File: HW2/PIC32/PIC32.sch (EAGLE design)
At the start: 23 parts, among them J4 AMP FCI 10103594-0001LF

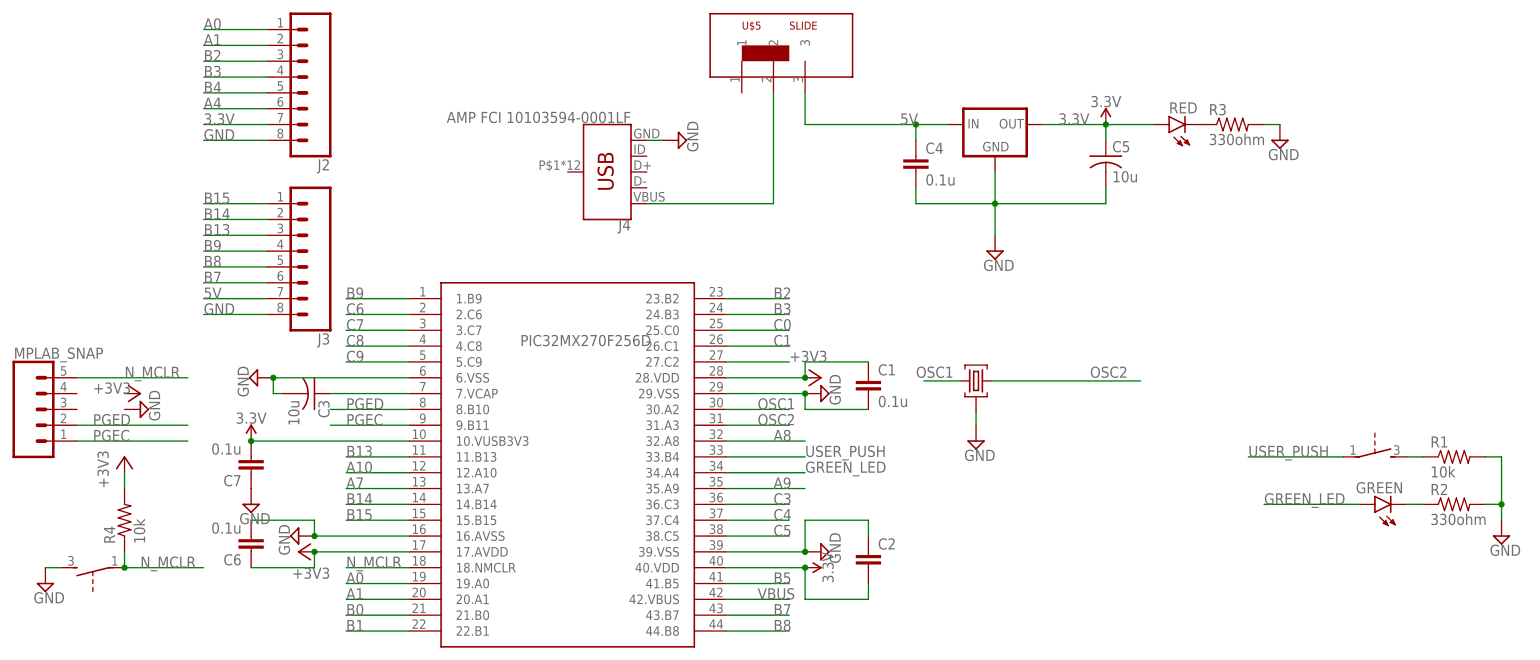
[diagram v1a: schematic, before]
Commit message: CAD images of wheel and box
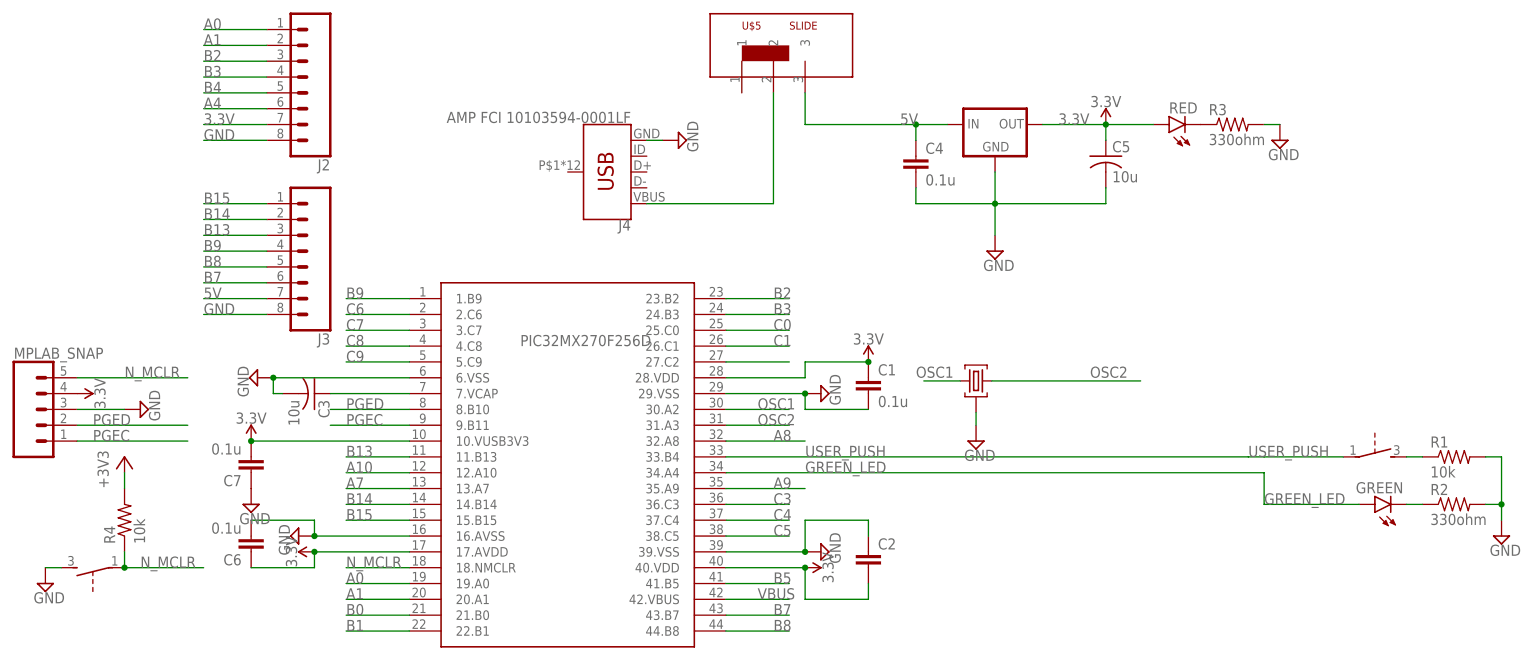
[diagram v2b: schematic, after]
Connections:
- removed net N$1: USER_PUSH.P
- removed net N$2: GREEN.A
- net +3V3: no longer C1.1, C6.1, U$1.17.AVDD, U$1.28.VDD
- net 3.3V: now also C1.1, C6.1, MPLAB_SNAP.4, U$1.17.AVDD, U$1.28.VDD
- net GND: now also MPLAB_SNAP.3
- net GREEN_LED: now also GREEN.A
- net USER_PUSH: now also USER_PUSH.P
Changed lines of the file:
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@@
 <part name="SUPPLY8" library="SparkFun-PowerSymbols" library_urn="urn:adsk.eagle:library:530" deviceset="3.3V" device=""/>
 <part name="SUPPLY9" library="supply2" library_urn="urn:adsk.eagle:library:372" deviceset="GND" device=""/>
-<part name="+3V1" library="supply1" library_urn="urn:adsk.eagle:library:371" deviceset="+3V3" device=""/>
 <part name="SUPPLY10" library="supply2" library_urn="urn:adsk.eagle:library:372" deviceset="GND" device=""/>
 <part name="C6" library="capacitor-wima" library_urn="urn:adsk.eagle:library:116" deviceset="C" device="2,5-3" package3d_urn="urn:adsk.eagle:package:5436/1" value="0.1u"/>
-<part name="+3V2" library="supply1" library_urn="urn:adsk.eagle:library:371" deviceset="+3V3" device=""/>
 <part name="R4" library="rcl" library_urn="urn:adsk.eagle:library:334" deviceset="R-US_" device="0207/7" package3d_urn="urn:adsk.eagle:package:23493/1" value="10k"/>
 <part name="SUPPLY11" library="supply2" library_urn="urn:adsk.eagle:library:372" deviceset="GND" device=""/>
@@
 <part name="SUPPLY12" library="supply2" library_urn="urn:adsk.eagle:library:372" deviceset="GND" device=""/>
 <part name="U$5" library="ME433" deviceset="SLIDE" device=""/>
-<part name="+3V3" library="supply1" library_urn="urn:adsk.eagle:library:371" deviceset="+3V3" device=""/>
 <part name="SUPPLY13" library="supply2" library_urn="urn:adsk.eagle:library:372" deviceset="GND" device=""/>
 <part name="+3V4" library="supply1" library_urn="urn:adsk.eagle:library:371" deviceset="+3V3" device=""/>
@@
 <part name="C7" library="capacitor-wima" library_urn="urn:adsk.eagle:library:116" deviceset="C" device="2,5-3" package3d_urn="urn:adsk.eagle:package:5436/1" value="0.1u"/>
 <part name="SUPPLY15" library="supply2" library_urn="urn:adsk.eagle:library:372" deviceset="GND" device=""/>
+<part name="SUPPLY16" library="SparkFun-PowerSymbols" library_urn="urn:adsk.eagle:library:530" deviceset="3.3V" device=""/>
+<part name="SUPPLY17" library="SparkFun-PowerSymbols" library_urn="urn:adsk.eagle:library:530" deviceset="3.3V" device=""/>
+<part name="SUPPLY18" library="SparkFun-PowerSymbols" library_urn="urn:adsk.eagle:library:530" deviceset="3.3V" device=""/>
 </parts>
 <sheets>
@@
 <attribute name="VALUE" x="43.815" y="-14.605" size="1.778" layer="96" rot="R90"/>
 </instance>
-<instance part="+3V1" gate="G$1" x="40.64" y="15.24" smashed="yes" rot="R270">
-<attribute name="VALUE" x="35.56" y="17.78" size="1.778" layer="96"/>
-</instance>
 <instance part="SUPPLY10" gate="GND" x="-43.18" y="-10.16" smashed="yes" rot="R270">
 <attribute name="VALUE" x="-46.355" y="-8.255" size="1.778" layer="96" rot="R270"/>
@@
 <attribute name="VALUE" x="-52.324" y="-8.001" size="1.778" layer="96" rot="R180"/>
 </instance>
-<instance part="+3V2" gate="G$1" x="-43.18" y="-12.7" smashed="yes" rot="R90">
-<attribute name="VALUE" x="-38.1" y="-15.24" size="1.778" layer="96" rot="R180"/>
-</instance>
 <instance part="R4" gate="G$1" x="-71.12" y="-7.62" smashed="yes" rot="R90">
 <attribute name="NAME" x="-72.6186" y="-11.43" size="1.778" layer="95" rot="R90"/>
@@
 <attribute name="VALUE" x="35.56" y="71.12" size="1.27" layer="94"/>
 </instance>
-<instance part="+3V3" gate="G$1" x="-68.58" y="12.7" smashed="yes" rot="R270">
-<attribute name="VALUE" x="-76.2" y="12.7" size="1.778" layer="96"/>
-</instance>
 <instance part="SUPPLY13" gate="GND" x="-68.58" y="10.16" smashed="yes" rot="R90">
 <attribute name="VALUE" x="-65.405" y="8.255" size="1.778" layer="96" rot="R90"/>
@@
 <instance part="SUPPLY15" gate="GND" x="-50.8" y="-5.08" smashed="yes">
 <attribute name="VALUE" x="-52.705" y="-8.255" size="1.778" layer="96"/>
+</instance>
+<instance part="SUPPLY16" gate="G$1" x="48.26" y="17.78" smashed="yes">
+<attribute name="VALUE" x="48.26" y="20.574" size="1.778" layer="96" align="bottom-center"/>
+</instance>
+<instance part="SUPPLY17" gate="G$1" x="-40.64" y="-12.7" smashed="yes" rot="R90">
+<attribute name="VALUE" x="-43.434" y="-12.7" size="1.778" layer="96" rot="R90" align="bottom-center"/>
+</instance>
+<instance part="SUPPLY18" gate="G$1" x="-78.74" y="12.7" smashed="yes" rot="R270">
+<attribute name="VALUE" x="-75.946" y="12.7" size="1.778" layer="96" rot="R270" align="bottom-center"/>
 </instance>
 </instances>
@@
 <label x="-58.42" y="25.4" size="1.778" layer="95"/>
 </segment>
-</net>
-<net name="N$2" class="0">
-<segment>
-<pinref part="GREEN" gate="G$1" pin="A"/>
-<wire x1="127" y1="-5.08" x2="111.76" y2="-5.08" width="0.1524" layer="91"/>
+<segment>
+<pinref part="MPLAB_SNAP" gate="G$1" pin="3"/>
+<pinref part="SUPPLY13" gate="GND" pin="GND"/>
+<wire x1="-78.74" y1="10.16" x2="-71.12" y2="10.16" width="0.1524" layer="91"/>
 </segment>
 </net>
@@
 <label x="-58.42" y="55.88" size="1.778" layer="95"/>
 </segment>
-</net>
-<net name="USER_PUSH" class="0">
-<segment>
-<pinref part="U$1" gate="G$1" pin="33.B4"/>
-<wire x1="25.4" y1="2.54" x2="38.1" y2="2.54" width="0.1524" layer="91"/>
-<label x="38.1" y="2.54" size="1.778" layer="95"/>
-<label x="109.22" y="2.54" size="1.778" layer="95"/>
-</segment>
-</net>
-<net name="GREEN_LED" class="0">
-<segment>
-<pinref part="U$1" gate="G$1" pin="34.A4"/>
-<wire x1="25.4" y1="0" x2="38.1" y2="0" width="0.1524" layer="91"/>
-<label x="38.1" y="0" size="1.778" layer="95"/>
-<label x="111.76" y="-5.08" size="1.778" layer="95"/>
-</segment>
-</net>
-<net name="N$1" class="0">
-<segment>
-<pinref part="USER_PUSH" gate="G$1" pin="P"/>
-<wire x1="124.46" y1="2.54" x2="109.22" y2="2.54" width="0.1524" layer="91"/>
-</segment>
-</net>
-<net name="+3V3" class="0">
 <segment>
 <pinref part="U$1" gate="G$1" pin="28.VDD"/>
-<wire x1="25.4" y1="15.24" x2="38.1" y2="15.24" width="0.1524" layer="91"/>
-<pinref part="+3V1" gate="G$1" pin="+3V3"/>
 <wire x1="38.1" y1="15.24" x2="38.1" y2="17.78" width="0.1524" layer="91"/>
-<junction x="38.1" y="15.24"/>
 <pinref part="C1" gate="G$1" pin="1"/>
 <wire x1="38.1" y1="17.78" x2="48.26" y2="17.78" width="0.1524" layer="91"/>
+<wire x1="25.4" y1="15.24" x2="38.1" y2="15.24" width="0.1524" layer="91"/>
+<pinref part="SUPPLY16" gate="G$1" pin="3.3V"/>
+<junction x="48.26" y="17.78"/>
 </segment>
 <segment>
 <wire x1="-25.4" y1="-12.7" x2="-40.64" y2="-12.7" width="0.1524" layer="91"/>
-<pinref part="+3V2" gate="G$1" pin="+3V3"/>
 <wire x1="-40.64" y1="-12.7" x2="-40.64" y2="-15.24" width="0.1524" layer="91"/>
-<junction x="-40.64" y="-12.7"/>
 <pinref part="C6" gate="G$1" pin="1"/>
 <wire x1="-40.64" y1="-15.24" x2="-50.8" y2="-15.24" width="0.1524" layer="91"/>
 <pinref part="U$1" gate="G$1" pin="17.AVDD"/>
-</segment>
+<pinref part="SUPPLY17" gate="G$1" pin="3.3V"/>
+<junction x="-40.64" y="-12.7"/>
+</segment>
+<segment>
+<pinref part="MPLAB_SNAP" gate="G$1" pin="4"/>
+<pinref part="SUPPLY18" gate="G$1" pin="3.3V"/>
+</segment>
+</net>
+<net name="USER_PUSH" class="0">
+<segment>
+<pinref part="U$1" gate="G$1" pin="33.B4"/>
+<label x="38.1" y="2.54" size="1.778" layer="95"/>
+<label x="109.22" y="2.54" size="1.778" layer="95"/>
+<pinref part="USER_PUSH" gate="G$1" pin="P"/>
+<wire x1="124.46" y1="2.54" x2="111.76" y2="2.54" width="0.1524" layer="91"/>
+<wire x1="111.76" y1="2.54" x2="109.22" y2="2.54" width="0.1524" layer="91"/>
+<wire x1="25.4" y1="2.54" x2="109.22" y2="2.54" width="0.1524" layer="91"/>
+</segment>
+</net>
+<net name="GREEN_LED" class="0">
+<segment>
+<pinref part="U$1" gate="G$1" pin="34.A4"/>
+<label x="38.1" y="0" size="1.778" layer="95"/>
+<label x="111.76" y="-5.08" size="1.778" layer="95"/>
+<pinref part="GREEN" gate="G$1" pin="A"/>
+<wire x1="127" y1="-5.08" x2="111.76" y2="-5.08" width="0.1524" layer="91"/>
+<wire x1="25.4" y1="0" x2="111.76" y2="0" width="0.1524" layer="91"/>
+<wire x1="111.76" y1="0" x2="111.76" y2="-5.08" width="0.1524" layer="91"/>
+</segment>
+</net>
+<net name="+3V3" class="0">
 <segment>
 <pinref part="+3V4" gate="G$1" pin="+3V3"/>

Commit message: HW15
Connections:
- removed net +3V3: R4.2
- net 3.3V: now also R4.2
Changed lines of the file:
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@@
 <part name="U$5" library="ME433" deviceset="SLIDE" device=""/>
 <part name="SUPPLY13" library="supply2" library_urn="urn:adsk.eagle:library:372" deviceset="GND" device=""/>
-<part name="+3V4" library="supply1" library_urn="urn:adsk.eagle:library:371" deviceset="+3V3" device=""/>
 <part name="SUPPLY14" library="SparkFun-PowerSymbols" library_urn="urn:adsk.eagle:library:530" deviceset="3.3V" device=""/>
 <part name="C7" library="capacitor-wima" library_urn="urn:adsk.eagle:library:116" deviceset="C" device="2,5-3" package3d_urn="urn:adsk.eagle:package:5436/1" value="0.1u"/>
@@
 <part name="SUPPLY17" library="SparkFun-PowerSymbols" library_urn="urn:adsk.eagle:library:530" deviceset="3.3V" device=""/>
 <part name="SUPPLY18" library="SparkFun-PowerSymbols" library_urn="urn:adsk.eagle:library:530" deviceset="3.3V" device=""/>
+<part name="SUPPLY19" library="SparkFun-PowerSymbols" library_urn="urn:adsk.eagle:library:530" deviceset="3.3V" device=""/>
 </parts>
 <sheets>
@@
 <attribute name="VALUE" x="-65.405" y="8.255" size="1.778" layer="96" rot="R90"/>
 </instance>
-<instance part="+3V4" gate="G$1" x="-71.12" y="2.54" smashed="yes">
-<attribute name="VALUE" x="-73.66" y="-2.54" size="1.778" layer="96" rot="R90"/>
-</instance>
 <instance part="SUPPLY14" gate="G$1" x="-50.8" y="5.08" smashed="yes">
 <attribute name="VALUE" x="-50.8" y="7.874" size="1.778" layer="96" align="bottom-center"/>
@@
 <instance part="SUPPLY18" gate="G$1" x="-78.74" y="12.7" smashed="yes" rot="R270">
 <attribute name="VALUE" x="-75.946" y="12.7" size="1.778" layer="96" rot="R270" align="bottom-center"/>
+</instance>
+<instance part="SUPPLY19" gate="G$1" x="-71.12" y="0" smashed="yes">
+<attribute name="VALUE" x="-71.12" y="2.794" size="1.778" layer="96" align="bottom-center"/>
 </instance>
 </instances>
@@
 <pinref part="SUPPLY18" gate="G$1" pin="3.3V"/>
 </segment>
+<segment>
+<pinref part="SUPPLY19" gate="G$1" pin="3.3V"/>
+<pinref part="R4" gate="G$1" pin="2"/>
+<wire x1="-71.12" y1="0" x2="-71.12" y2="-2.54" width="0.1524" layer="91"/>
+</segment>
 </net>
 <net name="USER_PUSH" class="0">
@@
 </segment>
 </net>
-<net name="+3V3" class="0">
-<segment>
-<pinref part="+3V4" gate="G$1" pin="+3V3"/>
-<pinref part="R4" gate="G$1" pin="2"/>
-<wire x1="-71.12" y1="0" x2="-71.12" y2="-2.54" width="0.1524" layer="91"/>
-</segment>
-</net>
